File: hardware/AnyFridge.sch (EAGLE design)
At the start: 11 parts

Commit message: Added 120 ohm resistor to board/schematic
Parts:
- added R2: 120OHM, SparkFun-Resistors:120OHM
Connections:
- removed net RED: ESP-1.33, LED-1.1
- new net RED-IN: ESP-1.33, R2.2
- new net RED-OUT: LED-1.1, R2.1
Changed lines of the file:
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@@
 <layer number="154" name="FabDoc2" color="7" fill="1" visible="no" active="no"/>
 <layer number="155" name="FabDoc3" color="7" fill="1" visible="no" active="no"/>
+<layer number="156" name="gesam-Maß" color="1" fill="7" visible="no" active="no"/>
+<layer number="157" name="FaceMchng" color="3" fill="1" visible="no" active="no"/>
+<layer number="158" name="FaceMMeas" color="3" fill="1" visible="no" active="no"/>
+<layer number="159" name="Geh-Bear2" color="1" fill="7" visible="no" active="no"/>
+<layer number="160" name="Topologie" color="9" fill="1" visible="no" active="no"/>
+<layer number="161" name="tomplace2" color="7" fill="1" visible="no" active="no"/>
 <layer number="166" name="AntennaArea" color="7" fill="1" visible="no" active="no"/>
 <layer number="168" name="4mmHeightArea" color="7" fill="1" visible="no" active="no"/>
@@
 <layer number="250" name="Descript" color="3" fill="1" visible="no" active="no"/>
 <layer number="251" name="SMDround" color="12" fill="11" visible="no" active="no"/>
+<layer number="252" name="BR-BS" color="7" fill="1" visible="no" active="no"/>
 <layer number="253" name="Extra" color="7" fill="1" visible="no" active="no"/>
 <layer number="254" name="cooling" color="7" fill="1" visible="no" active="no"/>
@@
 <schematic_group name="MCU" titleSize="2.54"/>
 <schematic_group name="SCANNER" titleSize="2.54"/>
-<schematic_group name="LED" titleSize="2.54"/>
+<schematic_group name="RED" titleSize="2.54"/>
 </groups>
 <parts>
@@
 <part name="TP_RX" library="testpad" library_urn="urn:adsk.eagle:library:385" deviceset="TP" device="PAD1-13" package3d_urn="urn:adsk.eagle:package:27946/1"/>
 <part name="TP_3.3V" library="testpad" library_urn="urn:adsk.eagle:library:385" deviceset="TP" device="PAD1-13" package3d_urn="urn:adsk.eagle:package:27946/1"/>
+<part name="R2" library="SparkFun-Resistors" deviceset="120OHM" device=""/>
 </parts>
 <sheets>
@@
 <attribute name="REV" x="236.22" y="6.604" size="2.7432" layer="94" font="vector"/>
 </instance>
-<instance part="LED-1" gate="A" x="35.56" y="83.82" smashed="yes" grouprefs="LED">
+<instance part="LED-1" gate="A" x="35.56" y="83.82" smashed="yes" grouprefs="RED">
 <attribute name="NAME" x="51.1556" y="95.4786" size="2.0828" layer="95" ratio="6" rot="SR0"/>
 <attribute name="VALUE" x="50.5206" y="92.9386" size="2.0828" layer="96" ratio="6" rot="SR0"/>
@@
 <attribute name="NAME" x="64.77" y="44.45" size="1.778" layer="95"/>
 <attribute name="TP_SIGNAL_NAME" x="67.31" y="41.91" size="1.778" layer="97"/>
+</instance>
+<instance part="R2" gate="G$1" x="81.28" y="81.28" smashed="yes">
+<attribute name="NAME" x="81.28" y="77.724" size="1.778" layer="95" font="vector" align="bottom-center"/>
+<attribute name="VALUE" x="81.28" y="77.216" size="1.778" layer="96" font="vector" align="top-center"/>
 </instance>
 </instances>
@@
 <segment>
 <pinref part="LED-1" gate="A" pin="2"/>
-<wire x1="35.56" y1="83.82" x2="33.02" y2="83.82" width="0.1524" layer="91" grouprefs="LED"/>
-<label x="33.02" y="83.82" size="1.778" layer="95" rot="R180" xref="yes" grouprefs="LED"/>
+<wire x1="35.56" y1="83.82" x2="33.02" y2="83.82" width="0.1524" layer="91" grouprefs="RED"/>
+<label x="33.02" y="83.82" size="1.778" layer="95" rot="R180" xref="yes" grouprefs="RED"/>
 </segment>
 <segment>
@@
 </segment>
 </net>
-<net name="RED" class="0">
-<segment>
-<pinref part="LED-1" gate="A" pin="1"/>
-<wire x1="76.2" y1="81.28" x2="78.74" y2="81.28" width="0.1524" layer="91" grouprefs="LED"/>
-<label x="78.74" y="81.28" size="1.27" layer="95" xref="yes" grouprefs="LED"/>
-</segment>
+<net name="RED-IN" class="0">
 <segment>
 <pinref part="ESP-1" gate="G$1" pin="33"/>
@@
 <label x="116.84" y="106.68" size="1.27" layer="95" rot="R180" xref="yes" grouprefs="MCU"/>
 </segment>
+<segment>
+<pinref part="R2" gate="G$1" pin="2"/>
+<wire x1="86.36" y1="81.28" x2="88.9" y2="81.28" width="0.1524" layer="91"/>
+<label x="88.9" y="81.28" size="1.778" layer="95" xref="yes"/>
+</segment>
 </net>
 <net name="BLUE" class="0">
 <segment>
 <pinref part="LED-1" gate="A" pin="3"/>
-<label x="78.74" y="83.82" size="1.27" layer="95" xref="yes" grouprefs="LED"/>
-<wire x1="76.2" y1="83.82" x2="78.74" y2="83.82" width="0.1524" layer="91" grouprefs="LED"/>
+<label x="78.74" y="83.82" size="1.27" layer="95" xref="yes" grouprefs="RED"/>
+<wire x1="76.2" y1="83.82" x2="78.74" y2="83.82" width="0.1524" layer="91" grouprefs="RED"/>
 </segment>
 <segment>
@@
 <segment>
 <pinref part="LED-1" gate="A" pin="4"/>
-<wire x1="76.2" y1="86.36" x2="78.74" y2="86.36" width="0.1524" layer="91" grouprefs="LED"/>
-<label x="78.74" y="86.36" size="1.27" layer="95" xref="yes" grouprefs="LED"/>
+<wire x1="76.2" y1="86.36" x2="78.74" y2="86.36" width="0.1524" layer="91" grouprefs="RED"/>
+<label x="78.74" y="86.36" size="1.27" layer="95" xref="yes" grouprefs="RED"/>
 </segment>
 <segment>
@@
 </segment>
 </net>
+<net name="RED-OUT" class="0">
+<segment>
+<pinref part="LED-1" gate="A" pin="1"/>
+<pinref part="R2" gate="G$1" pin="1"/>
+</segment>
+</net>

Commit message: schematic updated
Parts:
- R2: value 120OHM -> 68OHM-0603-1/10W-1%; device SparkFun-Resistors:120OHM -> SparkFun-Resistors:68OHM-0603-1/10W-1%
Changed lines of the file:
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@@
 <setting verticaltext="up"/>
 </settings>
-<grid distance="0.1" unitdist="inch" unit="inch" style="lines" multiple="1" display="no" altdistance="0.01" altunitdist="inch" altunit="inch"/>
+<grid distance="0.05" unitdist="inch" unit="inch" style="lines" multiple="1" display="no" altdistance="0.01" altunitdist="inch" altunit="inch"/>
 <layers>
 <layer number="1" name="Top" color="4" fill="1" visible="no" active="no"/>
@@
 <part name="TP_RX" library="testpad" library_urn="urn:adsk.eagle:library:385" deviceset="TP" device="PAD1-13" package3d_urn="urn:adsk.eagle:package:27946/1"/>
 <part name="TP_3.3V" library="testpad" library_urn="urn:adsk.eagle:library:385" deviceset="TP" device="PAD1-13" package3d_urn="urn:adsk.eagle:package:27946/1"/>
-<part name="R2" library="SparkFun-Resistors" deviceset="120OHM" device=""/>
+<part name="R2" library="SparkFun-Resistors" deviceset="68OHM" device="-0603-1/10W-1%"/>
 </parts>
 <sheets>
@@
 </instance>
 <instance part="R2" gate="G$1" x="81.28" y="81.28" smashed="yes">
-<attribute name="NAME" x="81.28" y="77.724" size="1.778" layer="95" font="vector" align="bottom-center"/>
-<attribute name="VALUE" x="81.28" y="77.216" size="1.778" layer="96" font="vector" align="top-center"/>
+<attribute name="NAME" x="81.28" y="77.47" size="1.778" layer="95" font="vector" align="bottom-center"/>
+<attribute name="VALUE" x="86.36" y="77.216" size="1.778" layer="96" font="vector" align="top-center"/>
 </instance>
 </instances>
@@
 </segment>
 <segment>
-<pinref part="R2" gate="G$1" pin="2"/>
 <wire x1="86.36" y1="81.28" x2="88.9" y2="81.28" width="0.1524" layer="91"/>
 <label x="88.9" y="81.28" size="1.778" layer="95" xref="yes"/>
-</segment>
-</net>
+<pinref part="R2" gate="G$1" pin="2"/>
+</segment>
+</net>

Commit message: Add Green and Blue resistors
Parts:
- added R3, R4: 22Ω, SparkFun-Resistors:22OHM-0603-1/10W-1%
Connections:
- net RED-IN renamed RED
- new net N$2: LED-1.4, R3.1
- new net N$3: LED-1.3, R4.1
- net BLUE: now also R4.2; no longer LED-1.3
- net GREEN: now also R3.2; no longer LED-1.4
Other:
- moved on the sheet: LED-1, R2

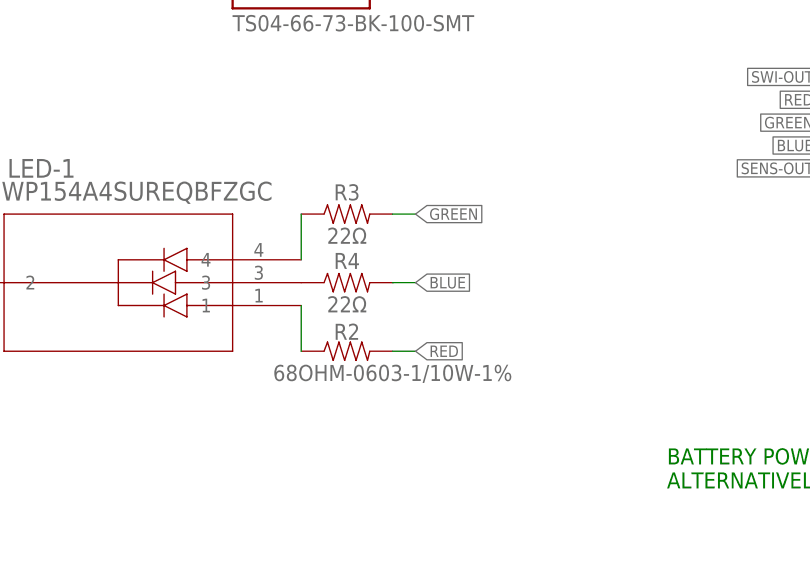
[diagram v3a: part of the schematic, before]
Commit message: Put project name + revision in silkscreen, rename resistor to LED pins
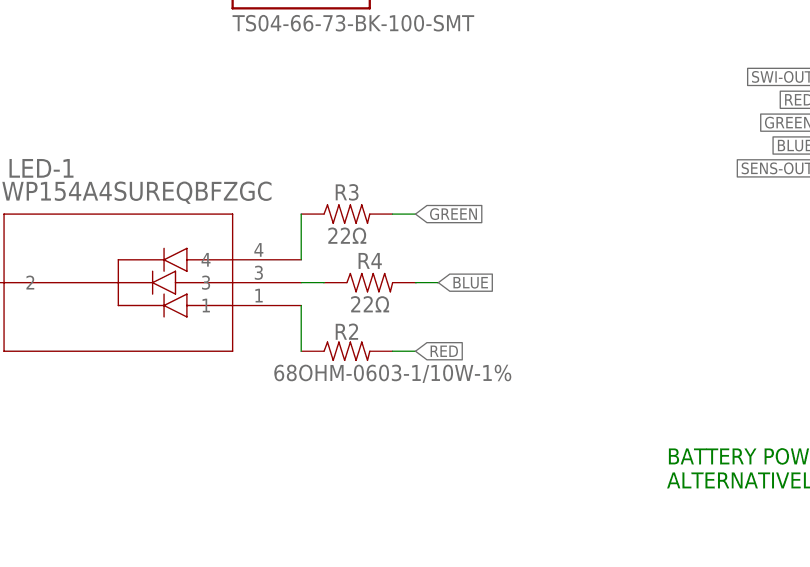
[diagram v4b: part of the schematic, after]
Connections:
- net N$2 renamed GREEN-IN
- net N$3 renamed BLUE-IN
- net RED-OUT renamed RED-IN
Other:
- moved on the sheet: R4
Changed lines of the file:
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@@
 <attribute name="VALUE" x="63.5" y="92.456" size="1.778" layer="96" font="vector" align="top-center"/>
 </instance>
-<instance part="R4" gate="G$1" x="63.5" y="86.36" smashed="yes">
-<attribute name="NAME" x="63.5" y="87.884" size="1.778" layer="95" font="vector" align="bottom-center"/>
-<attribute name="VALUE" x="63.5" y="84.836" size="1.778" layer="96" font="vector" align="top-center"/>
+<instance part="R4" gate="G$1" x="66.04" y="86.36" smashed="yes">
+<attribute name="NAME" x="66.04" y="87.884" size="1.778" layer="95" font="vector" align="bottom-center"/>
+<attribute name="VALUE" x="66.04" y="84.836" size="1.778" layer="96" font="vector" align="top-center"/>
 </instance>
 </instances>
@@
 <net name="BLUE" class="0">
 <segment>
-<label x="71.12" y="86.36" size="1.27" layer="95" xref="yes" grouprefs="LED"/>
-<pinref part="R4" gate="G$1" pin="2"/>
-<wire x1="68.58" y1="86.36" x2="71.12" y2="86.36" width="0.1524" layer="91" grouprefs="LED"/>
-</segment>
-<segment>
 <pinref part="ESP-1" gate="G$1" pin="12"/>
 <wire x1="119.38" y1="101.6" x2="116.84" y2="101.6" width="0.1524" layer="91" grouprefs="MCU"/>
 <label x="116.84" y="101.6" size="1.27" layer="95" rot="R180" xref="yes" grouprefs="MCU"/>
 </segment>
+<segment>
+<pinref part="R4" gate="G$1" pin="2"/>
+<wire x1="71.12" y1="86.36" x2="73.66" y2="86.36" width="0.1524" layer="91"/>
+<label x="73.66" y="86.36" size="1.27" layer="95" xref="yes"/>
+</segment>
 </net>
 <net name="GREEN" class="0">
@@
 </segment>
 </net>
-<net name="RED-OUT" class="0">
+<net name="RED-IN" class="0">
 <segment>
 <pinref part="LED-1" gate="A" pin="1"/>
@@
 </segment>
 </net>
-<net name="N$2" class="0">
+<net name="GREEN-IN" class="0">
 <segment>
 <pinref part="LED-1" gate="A" pin="4"/>
@@
 </segment>
 </net>
-<net name="N$3" class="0">
+<net name="BLUE-IN" class="0">
 <segment>
 <pinref part="LED-1" gate="A" pin="3"/>
 <pinref part="R4" gate="G$1" pin="1"/>
-</segment>
-</net>
+<wire x1="60.96" y1="86.36" x2="58.42" y2="86.36" width="0.1524" layer="91"/>
+</segment>
+</net>
